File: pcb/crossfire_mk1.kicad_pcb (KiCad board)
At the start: 2 copper layers, 59.6 x 57.8 mm, 72 parts, among them J1 USB_C_Receptacle_USB2.0, J2 USB_A, J3 USB_A, J4 USB_A, J5 USB_A, J6 Conn_01x05, J7 Conn_01x07, SW1 SW_Push_Dual, U1 W25Q16JVUXIQ_TR, U2 RP2040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

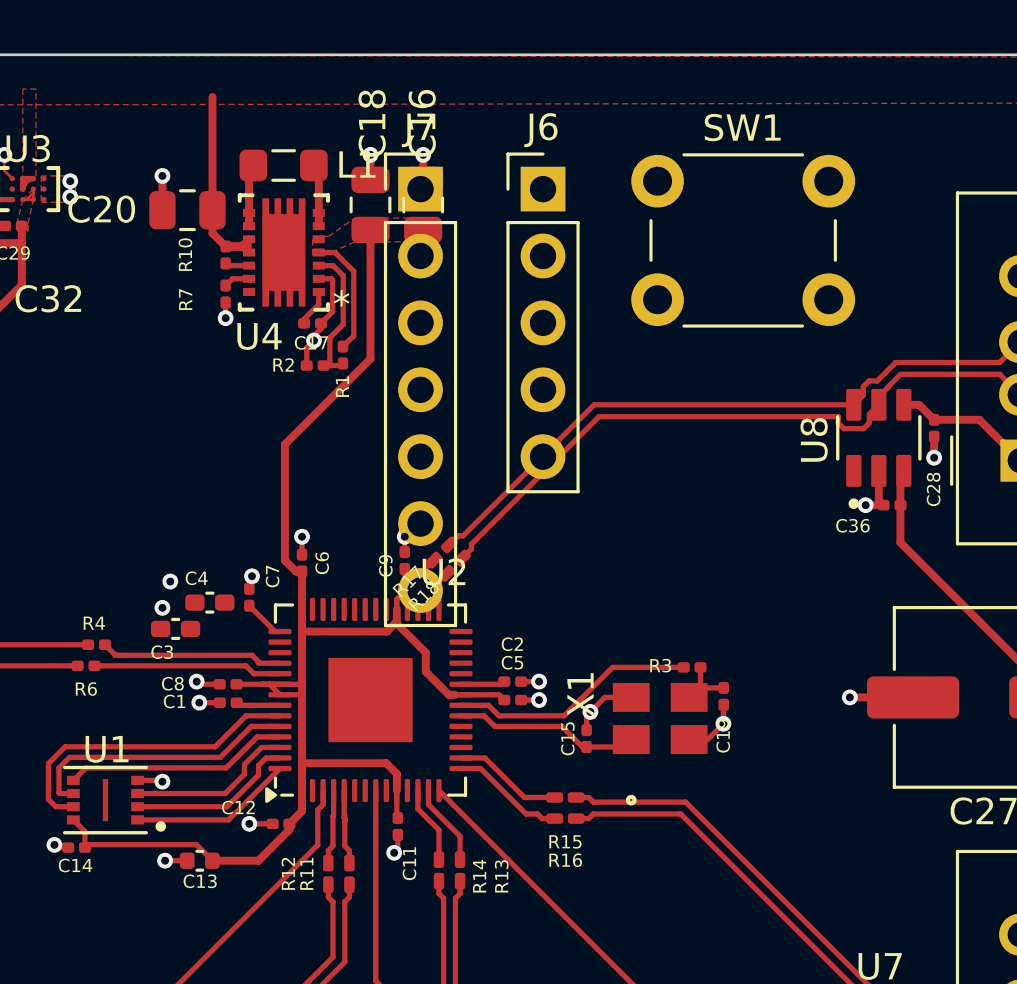
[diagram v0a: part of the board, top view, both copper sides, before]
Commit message: integrate debug and oled connectors
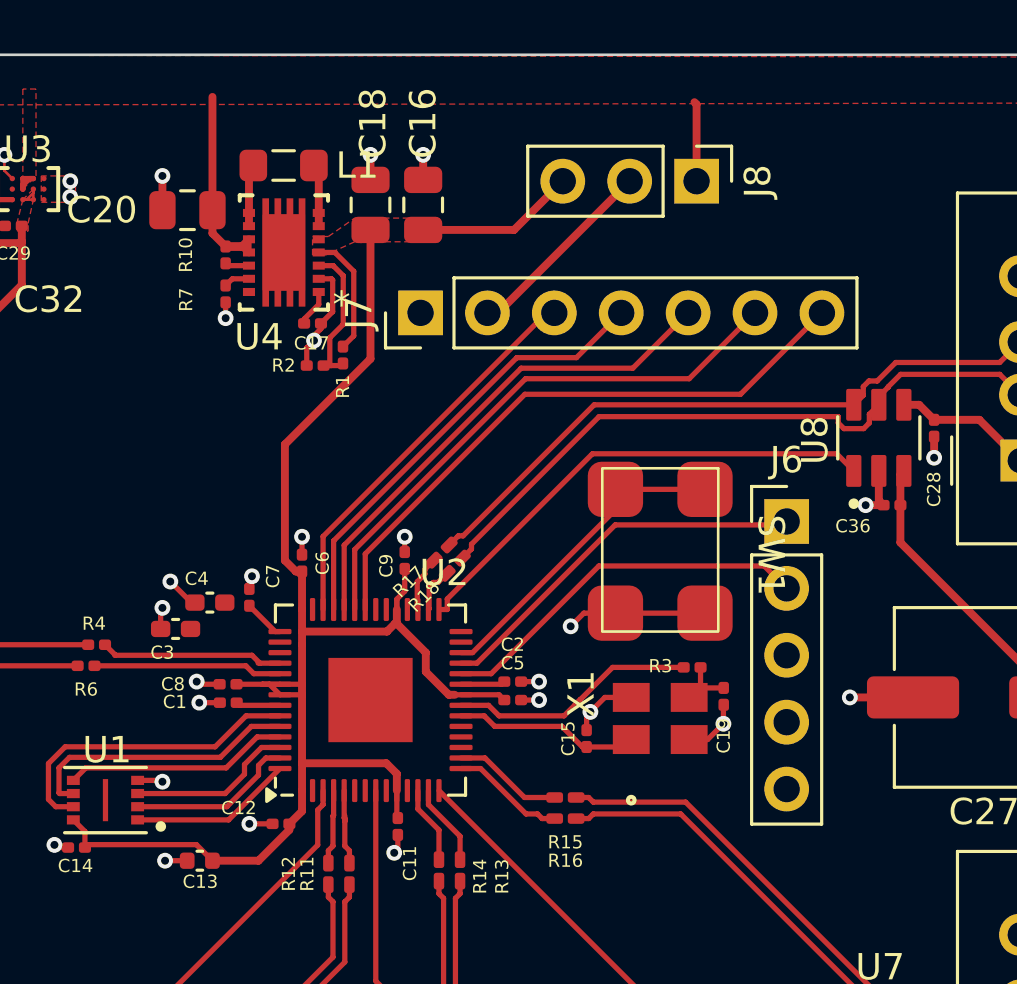
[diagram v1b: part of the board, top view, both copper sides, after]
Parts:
- added J8: OLED_PWR_JMP, Connector_PinHeader_2.54mm:PinHeader_1x03_P2.54mm_Vertical, F.Cu at (91.6, 77.0)
- J6: value Conn_01x05 -> DEBUG_CONN
- J7: value Conn_01x07 -> OLED_CONN
- SW1: value SW_Push_Dual -> SW_RESET; footprint Button_Switch_THT:SW_PUSH_6mm -> project-fooprints:Sumida_CPFC6D36NP-100M06
- moved J6 15.6 mm to (95.0, 89.9)
- moved SW1 14.0 mm to (90.3, 91.0), turned to -90 degrees
- moved J7 4.70 mm to (81.1, 82.0), turned to 90 degrees
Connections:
- J6 pad 1: /swd_clk -> /swd_io
- J6 pad 2: /swd_io -> /swd_clk
- J7 pad 2: +5V -> /oled_pwr
- U2 pad 27: /usb4_vben -> unconnected-(U2-GPIO16-Pad27)
- U2 pad 29: unconnected-(U2-GPIO18-Pad29) -> /usb4_vben
- U2 pad 35: unconnected-(U2-GPIO23-Pad35) -> /led_status
- U2 pad 36: /usbc1_vbus_pres -> /oled_cs
- U2 pad 37: /led_status -> /oled_dc
- U2 pad 38: unconnected-(U2-GPIO26_ADC0-Pad38) -> /oled_reset
- U2 pad 39: unconnected-(U2-GPIO27_ADC1-Pad39) -> /oled_data
- U2 pad 40: unconnected-(U2-GPIO28_ADC2-Pad40) -> /oled_clk
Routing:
- net /oled_cs: track 0.00 -> 23.2 mm
- net /oled_dc: track 0.00 -> 21.2 mm
- net /oled_reset: track 0.00 -> 19.2 mm
- net /usb4_vben: track 0.31 -> 19.0 mm
- net /oled_data: track 0.00 -> 17.1 mm
- net /oled_clk: track 0.00 -> 15.1 mm
- net /swd_io: track 0.00 -> 14.6 mm
- net /swd_clk: track 0.00 -> 14.5 mm
- net /mcu_run: track 0.00 -> 12.3 mm
- net /oled_pwr: track 0.00 -> 7.47 mm
- net GND: track 49.4 -> 56.8 mm, vias 40 -> 41
- net +3.3V: track 62.4 -> 68.5 mm
- net +5V: track 88.1 -> 91.2 mm
